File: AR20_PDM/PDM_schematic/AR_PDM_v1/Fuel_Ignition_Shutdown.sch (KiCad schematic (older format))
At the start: 22 parts, among them K1 DIPxx-1Cxx-51x, K2 DIPxx-1Cxx-51x, U11 N-MOS, U12 P-MOS, U13 N-MOS, U14 N-MOS, U29 INA233, U30 INA233

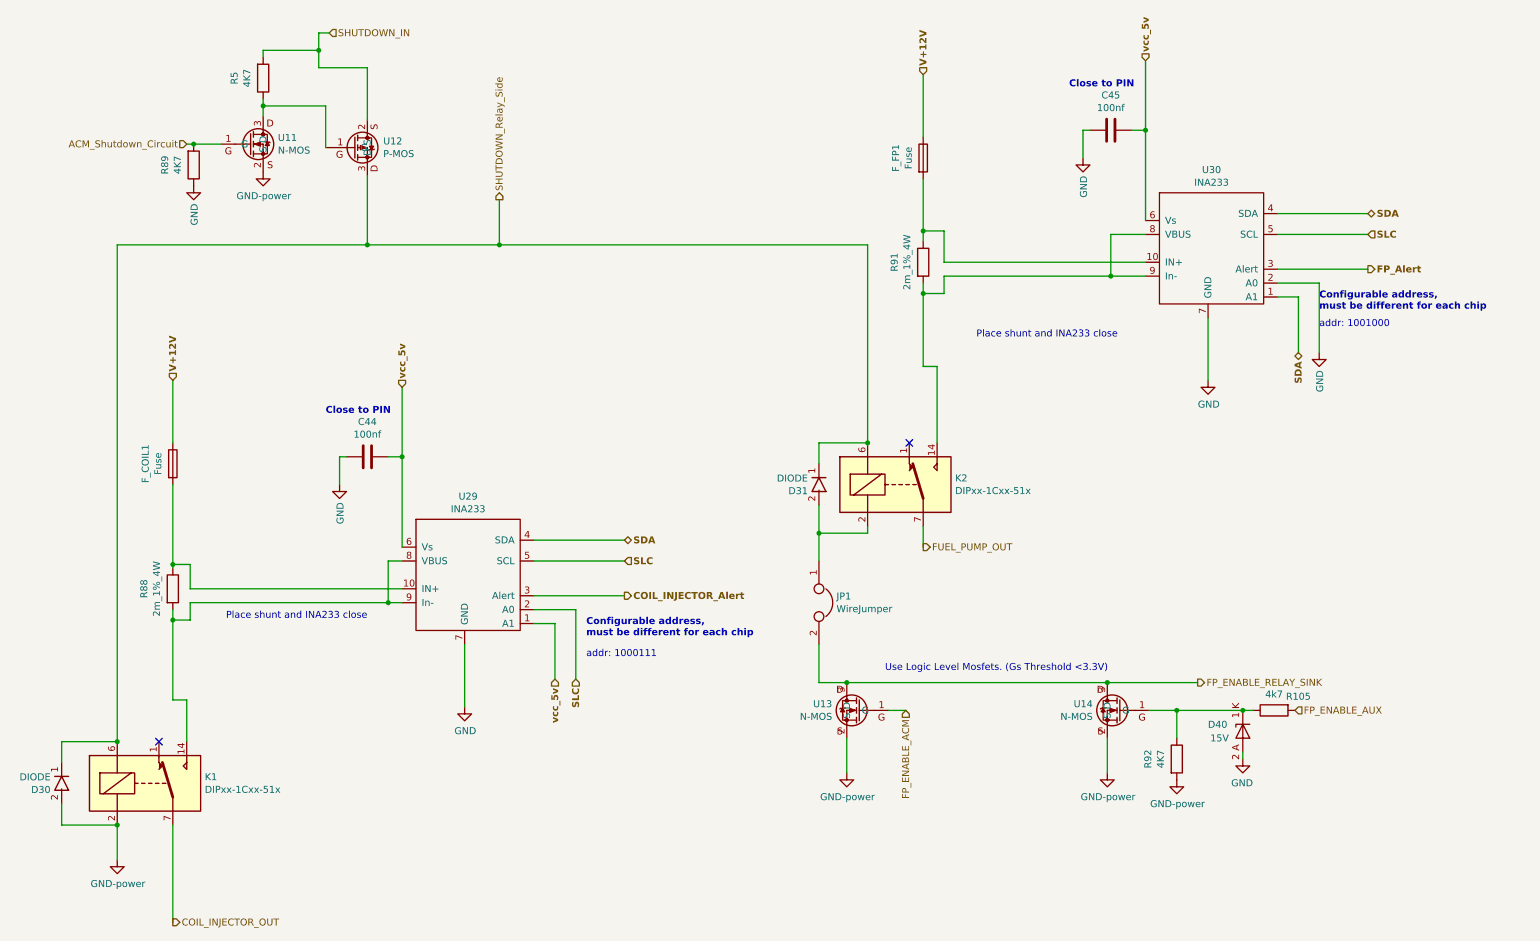
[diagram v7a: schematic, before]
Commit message: schematics rework
Fixed INA233 frying due to inductive flyback:
- Paced ina233 high side of the mosftets
- New input protection reseistors, and zener diodes, on each ina233.
Simplified:
- Removed the MUX and mos sense lines, as i realize that most of this functionality can be obtained trough INA233.
- Removed some of the cappacitors , besides the most needed ones.
- removed  back to back zener diode configuration, now a single diode insted.
 to reduce negative voltage in case of loss of VS, to be easy on the INA233 filters.
new stuff:
- Another temp sensor.
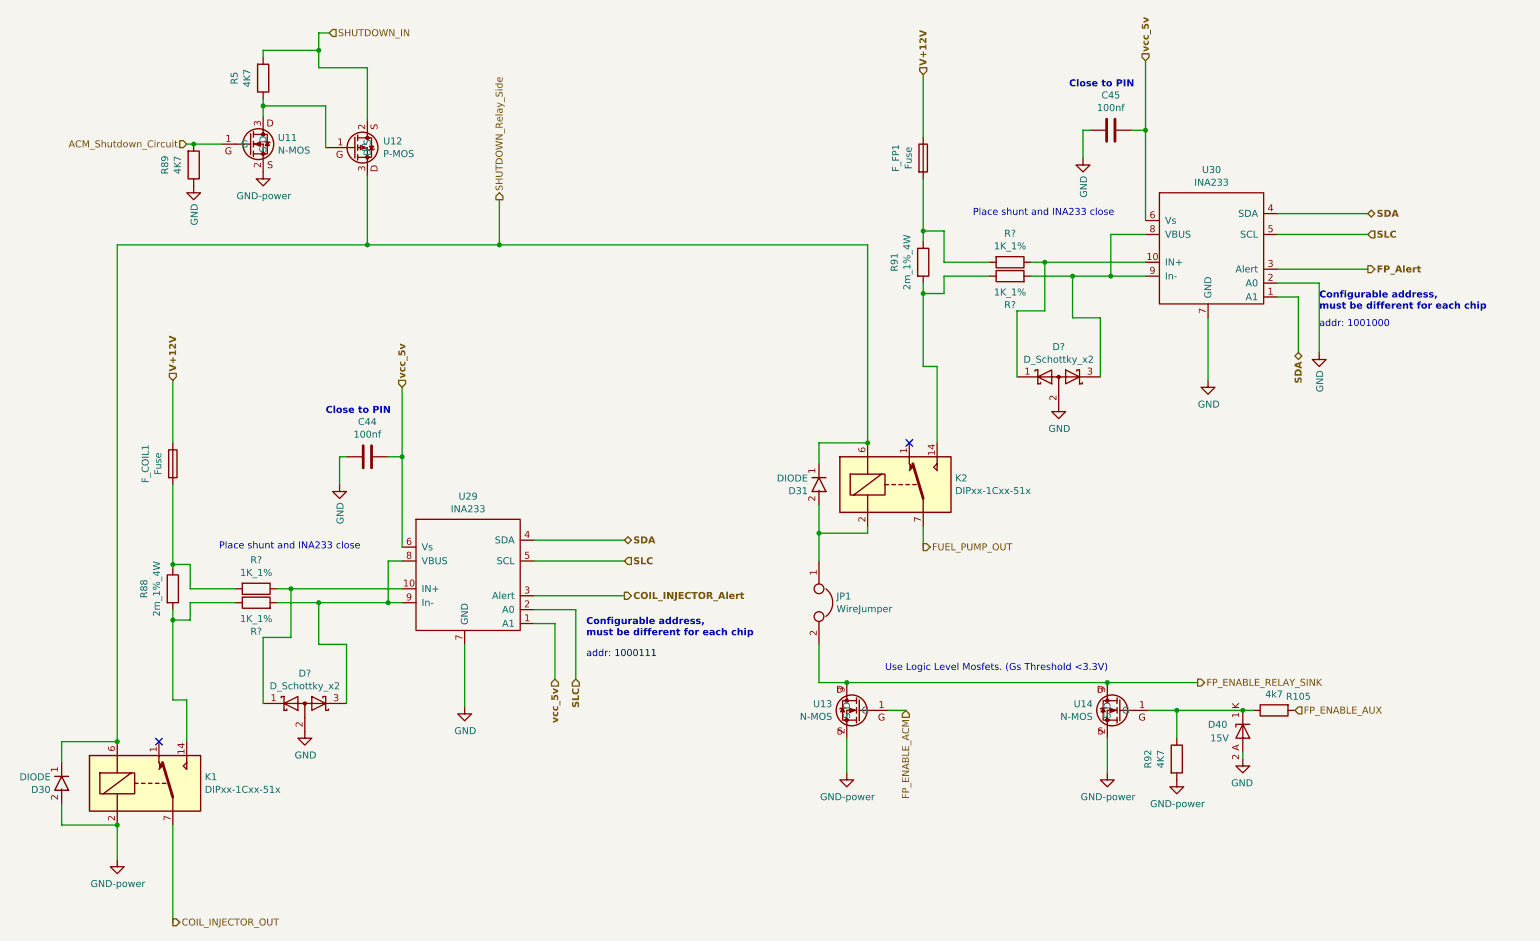
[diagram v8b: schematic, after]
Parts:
- added D? (x2): D_Schottky_x2, symbol AR20_PDM_v1-rescue:D_Schottky_x2
- added R? (x4): 1K_1%, Resistor_SMD:R_0603_1608Metric, symbol AR20_PDM_v1-rescue:R-Device
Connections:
- net GND: now also D?.2 (A), D?.2 (A)
- net at F_FP1.2, R91.1: now also R?.2; no longer U30.10 (IN+)
- net at F_COIL1.2, R88.1: now also R?.2; no longer U29.10 (IN+)
- net at U29.8 (VBUS), U29.9 (In-): now also D?.3 (K), R?.2; no longer K1.14, R88.2
- net at U30.8 (VBUS), U30.9 (In-): now also D?.3 (K), R?.2; no longer K2.14, R91.2
- new net: D?.1 (K), R?.1, U29.10 (IN+)
- new net: D?.1 (K), R?.1, U30.10 (IN+)
- new net: K2.14, R91.2, R?.1
- new net: K1.14, R88.2, R?.1
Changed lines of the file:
@@
 $Descr A4 11693 8268
 encoding utf-8
-Sheet 10 14
+Sheet 9 13
 Title ""
 Date ""
@@
 Wire Wire Line
 	1950 3650 1950 3200
-Text Notes 8750 2900 2    50   ~ 0
+Text Notes 8725 2025 2    50   ~ 0
 Place shunt and INA233 close \n
 Text HLabel 10025 5575 2    50   Input ~ 0
@@
 Text Notes 7075 5300 0    50   ~ 0
 Use Logic Level Mosfets. (Gs Threshold <3.3V)
-Text Notes 3350 4925 2    50   ~ 0
+Text Notes 3300 4425 2    50   ~ 0
 Place shunt and INA233 close \n
 Text HLabel 1950 3200 1    50   Input ~ 10
@@
 	1950 4925 1950 5500
 Wire Wire Line
-	3600 4700 2075 4700
-Wire Wire Line
 	2075 4700 2075 4525
 Wire Wire Line
@@
 Wire Wire Line
 	3500 4500 3500 4800
-Connection ~ 3500 4800
-Wire Wire Line
-	3500 4800 2075 4800
-Wire Wire Line
-	8950 2350 7500 2350
 Wire Wire Line
 	7500 2350 7500 2125
@@
 Wire Wire Line
 	8700 2150 8700 2450
-Connection ~ 8700 2450
-Wire Wire Line
-	8700 2450 7500 2450
 Text HLabel 7225 5575 3    50   Input ~ 0
 FP_ENABLE_ACM
@@
 Wire Wire Line
 	3350 950  3350 1325
+$Comp
+L AR20_PDM_v1-rescue:D_Schottky_x2 D?
+U 1 1 5EEF3E48
+P 8325 3175
+AR Path="/5DA89415/5EEF3E48" Ref="D?"  Part="1"
+AR Path="/5E10174B/5EEF3E48" Ref="D?"  Part="1"
+F 0 "D?" H 8325 3391 50  0000 C CNN
+F 1 "D_Schottky_x2" H 8325 3300 50  0000 C CNN
+F 2 "" H 8325 3175 50  0001 C CNN
+F 3 "~" H 8325 3175 50  0001 C CNN
+	1    8325 3175
+	1    0    0    -1
+$EndComp
+$Comp
+L AR20_PDM_v1-rescue:GND-power #PWR?
+U 1 1 5EEF3E4E
+P 8325 3375
+AR Path="/5DA89415/5EEF3E4E" Ref="#PWR?"  Part="1"
+AR Path="/5DEB10A1/5EEF3E4E" Ref="#PWR?"  Part="1"
+AR Path="/5DEB20EA/5EEF3E4E" Ref="#PWR?"  Part="1"
+AR Path="/5E0E4725/5EEF3E4E" Ref="#PWR?"  Part="1"
+AR Path="/5E0E4A93/5EEF3E4E" Ref="#PWR?"  Part="1"
+AR Path="/5E0E4EB5/5EEF3E4E" Ref="#PWR?"  Part="1"
+AR Path="/5E0E5304/5EEF3E4E" Ref="#PWR?"  Part="1"
+AR Path="/5E0E594B/5EEF3E4E" Ref="#PWR?"  Part="1"
+AR Path="/5E0E607C/5EEF3E4E" Ref="#PWR?"  Part="1"
+AR Path="/5E0FB5C8/5EEF3E4E" Ref="#PWR?"  Part="1"
+AR Path="/5E0FBBBD/5EEF3E4E" Ref="#PWR?"  Part="1"
+AR Path="/5E0FC3A2/5EEF3E4E" Ref="#PWR?"  Part="1"
+AR Path="/5E0FCFDC/5EEF3E4E" Ref="#PWR?"  Part="1"
+AR Path="/5E0FDCCC/5EEF3E4E" Ref="#PWR?"  Part="1"
+AR Path="/5E10174B/5EEF3E4E" Ref="#PWR?"  Part="1"
+F 0 "#PWR?" H 8325 3125 50  0001 C CNN
+F 1 "GND" H 8330 3202 50  0000 C CNN
+F 2 "" H 8325 3375 50  0001 C CNN
+F 3 "" H 8325 3375 50  0001 C CNN
+	1    8325 3375
+	1    0    0    -1
+$EndComp
+$Comp
+L AR20_PDM_v1-rescue:R-Device R?
+U 1 1 5EEF3E55
+P 7975 2350
+AR Path="/5DA89415/5EEF3E55" Ref="R?"  Part="1"
+AR Path="/5DEB10A1/5EEF3E55" Ref="R?"  Part="1"
+AR Path="/5DEB20EA/5EEF3E55" Ref="R?"  Part="1"
+AR Path="/5E0E4725/5EEF3E55" Ref="R?"  Part="1"
+AR Path="/5E0E4A93/5EEF3E55" Ref="R?"  Part="1"
+AR Path="/5E0E4EB5/5EEF3E55" Ref="R?"  Part="1"
+AR Path="/5E0E5304/5EEF3E55" Ref="R?"  Part="1"
+AR Path="/5E0E594B/5EEF3E55" Ref="R?"  Part="1"
+AR Path="/5E0E607C/5EEF3E55" Ref="R?"  Part="1"
+AR Path="/5E0FB5C8/5EEF3E55" Ref="R?"  Part="1"
+AR Path="/5E0FBBBD/5EEF3E55" Ref="R?"  Part="1"
+AR Path="/5E0FC3A2/5EEF3E55" Ref="R?"  Part="1"
+AR Path="/5E0FCFDC/5EEF3E55" Ref="R?"  Part="1"
+AR Path="/5E0FDCCC/5EEF3E55" Ref="R?"  Part="1"
+AR Path="/5E10174B/5EEF3E55" Ref="R?"  Part="1"
+F 0 "R?" V 7768 2350 50  0000 C CNN
+F 1 "1K_1%" V 7859 2350 50  0000 C CNN
+F 2 "Resistor_SMD:R_0603_1608Metric" V 7905 2350 50  0001 C CNN
+F 3 "~" H 7975 2350 50  0001 C CNN
+	1    7975 2350
+	0    1    1    0
+$EndComp
+$Comp
+L AR20_PDM_v1-rescue:R-Device R?
+U 1 1 5EEF3E5E
+P 7975 2450
+AR Path="/5DA89415/5EEF3E5E" Ref="R?"  Part="1"
+AR Path="/5DEB10A1/5EEF3E5E" Ref="R?"  Part="1"
+AR Path="/5DEB20EA/5EEF3E5E" Ref="R?"  Part="1"
+AR Path="/5E0E4725/5EEF3E5E" Ref="R?"  Part="1"
+AR Path="/5E0E4A93/5EEF3E5E" Ref="R?"  Part="1"
+AR Path="/5E0E4EB5/5EEF3E5E" Ref="R?"  Part="1"
+AR Path="/5E0E5304/5EEF3E5E" Ref="R?"  Part="1"
+AR Path="/5E0E594B/5EEF3E5E" Ref="R?"  Part="1"
+AR Path="/5E0E607C/5EEF3E5E" Ref="R?"  Part="1"
+AR Path="/5E0FB5C8/5EEF3E5E" Ref="R?"  Part="1"
+AR Path="/5E0FBBBD/5EEF3E5E" Ref="R?"  Part="1"
+AR Path="/5E0FC3A2/5EEF3E5E" Ref="R?"  Part="1"
+AR Path="/5E0FCFDC/5EEF3E5E" Ref="R?"  Part="1"
+AR Path="/5E0FDCCC/5EEF3E5E" Ref="R?"  Part="1"
+AR Path="/5E10174B/5EEF3E5E" Ref="R?"  Part="1"
+F 0 "R?" V 7768 2450 50  0000 C CNN
+F 1 "1K_1%" V 7859 2450 50  0000 C CNN
+F 2 "Resistor_SMD:R_0603_1608Metric" V 7905 2450 50  0001 C CNN
+F 3 "~" H 7975 2450 50  0001 C CNN
+	1    7975 2450
+	0    -1   -1   0
+$EndComp
+Connection ~ 8700 2450
+Wire Wire Line
+	8700 2450 8425 2450
+Wire Wire Line
+	8950 2350 8225 2350
+Wire Wire Line
+	7825 2350 7500 2350
+Wire Wire Line
+	7825 2450 7500 2450
+Wire Wire Line
+	8025 3175 8025 2700
+Wire Wire Line
+	8025 2700 8225 2700
+Wire Wire Line
+	8225 2700 8225 2350
+Connection ~ 8225 2350
+Wire Wire Line
+	8225 2350 8125 2350
+Wire Wire Line
+	8625 3175 8625 2750
+Wire Wire Line
+	8625 2750 8425 2750
+Wire Wire Line
+	8425 2750 8425 2450
+Connection ~ 8425 2450
+Wire Wire Line
+	8425 2450 8125 2450
+$Comp
+L AR20_PDM_v1-rescue:D_Schottky_x2 D?
+U 1 1 5EF32925
+P 2900 5525
+AR Path="/5DA89415/5EF32925" Ref="D?"  Part="1"
+AR Path="/5E10174B/5EF32925" Ref="D?"  Part="1"
+F 0 "D?" H 2900 5741 50  0000 C CNN
+F 1 "D_Schottky_x2" H 2900 5650 50  0000 C CNN
+F 2 "" H 2900 5525 50  0001 C CNN
+F 3 "~" H 2900 5525 50  0001 C CNN
+	1    2900 5525
+	1    0    0    -1
+$EndComp
+$Comp
+L AR20_PDM_v1-rescue:GND-power #PWR?
+U 1 1 5EF3292B
+P 2900 5725
+AR Path="/5DA89415/5EF3292B" Ref="#PWR?"  Part="1"
+AR Path="/5DEB10A1/5EF3292B" Ref="#PWR?"  Part="1"
+AR Path="/5DEB20EA/5EF3292B" Ref="#PWR?"  Part="1"
+AR Path="/5E0E4725/5EF3292B" Ref="#PWR?"  Part="1"
+AR Path="/5E0E4A93/5EF3292B" Ref="#PWR?"  Part="1"
+AR Path="/5E0E4EB5/5EF3292B" Ref="#PWR?"  Part="1"
+AR Path="/5E0E5304/5EF3292B" Ref="#PWR?"  Part="1"
+AR Path="/5E0E594B/5EF3292B" Ref="#PWR?"  Part="1"
+AR Path="/5E0E607C/5EF3292B" Ref="#PWR?"  Part="1"
+AR Path="/5E0FB5C8/5EF3292B" Ref="#PWR?"  Part="1"
+AR Path="/5E0FBBBD/5EF3292B" Ref="#PWR?"  Part="1"
+AR Path="/5E0FC3A2/5EF3292B" Ref="#PWR?"  Part="1"
+AR Path="/5E0FCFDC/5EF3292B" Ref="#PWR?"  Part="1"
+AR Path="/5E0FDCCC/5EF3292B" Ref="#PWR?"  Part="1"
+AR Path="/5E10174B/5EF3292B" Ref="#PWR?"  Part="1"
+F 0 "#PWR?" H 2900 5475 50  0001 C CNN
+F 1 "GND" H 2905 5552 50  0000 C CNN
+F 2 "" H 2900 5725 50  0001 C CNN
+F 3 "" H 2900 5725 50  0001 C CNN
+	1    2900 5725
+	1    0    0    -1
+$EndComp
+$Comp
+L AR20_PDM_v1-rescue:R-Device R?
+U 1 1 5EF32931
+P 2550 4700
+AR Path="/5DA89415/5EF32931" Ref="R?"  Part="1"
+AR Path="/5DEB10A1/5EF32931" Ref="R?"  Part="1"
+AR Path="/5DEB20EA/5EF32931" Ref="R?"  Part="1"
+AR Path="/5E0E4725/5EF32931" Ref="R?"  Part="1"
+AR Path="/5E0E4A93/5EF32931" Ref="R?"  Part="1"
+AR Path="/5E0E4EB5/5EF32931" Ref="R?"  Part="1"
+AR Path="/5E0E5304/5EF32931" Ref="R?"  Part="1"
+AR Path="/5E0E594B/5EF32931" Ref="R?"  Part="1"
+AR Path="/5E0E607C/5EF32931" Ref="R?"  Part="1"
+AR Path="/5E0FB5C8/5EF32931" Ref="R?"  Part="1"
+AR Path="/5E0FBBBD/5EF32931" Ref="R?"  Part="1"
+AR Path="/5E0FC3A2/5EF32931" Ref="R?"  Part="1"
+AR Path="/5E0FCFDC/5EF32931" Ref="R?"  Part="1"
+AR Path="/5E0FDCCC/5EF32931" Ref="R?"  Part="1"
+AR Path="/5E10174B/5EF32931" Ref="R?"  Part="1"
+F 0 "R?" V 2343 4700 50  0000 C CNN
+F 1 "1K_1%" V 2434 4700 50  0000 C CNN
+F 2 "Resistor_SMD:R_0603_1608Metric" V 2480 4700 50  0001 C CNN
+F 3 "~" H 2550 4700 50  0001 C CNN
+	1    2550 4700
+	0    1    1    0
+$EndComp
+$Comp
+L AR20_PDM_v1-rescue:R-Device R?
+U 1 1 5EF32937
+P 2550 4800
+AR Path="/5DA89415/5EF32937" Ref="R?"  Part="1"
+AR Path="/5DEB10A1/5EF32937" Ref="R?"  Part="1"
+AR Path="/5DEB20EA/5EF32937" Ref="R?"  Part="1"
+AR Path="/5E0E4725/5EF32937" Ref="R?"  Part="1"
+AR Path="/5E0E4A93/5EF32937" Ref="R?"  Part="1"
+AR Path="/5E0E4EB5/5EF32937" Ref="R?"  Part="1"
+AR Path="/5E0E5304/5EF32937" Ref="R?"  Part="1"
+AR Path="/5E0E594B/5EF32937" Ref="R?"  Part="1"
+AR Path="/5E0E607C/5EF32937" Ref="R?"  Part="1"
+AR Path="/5E0FB5C8/5EF32937" Ref="R?"  Part="1"
+AR Path="/5E0FBBBD/5EF32937" Ref="R?"  Part="1"
+AR Path="/5E0FC3A2/5EF32937" Ref="R?"  Part="1"
+AR Path="/5E0FCFDC/5EF32937" Ref="R?"  Part="1"
+AR Path="/5E0FDCCC/5EF32937" Ref="R?"  Part="1"
+AR Path="/5E10174B/5EF32937" Ref="R?"  Part="1"
+F 0 "R?" V 2343 4800 50  0000 C CNN
+F 1 "1K_1%" V 2434 4800 50  0000 C CNN
+F 2 "Resistor_SMD:R_0603_1608Metric" V 2480 4800 50  0001 C CNN
+F 3 "~" H 2550 4800 50  0001 C CNN
+	1    2550 4800
+	0    -1   -1   0
+$EndComp
+Wire Wire Line
+	2400 4700 2075 4700
+Wire Wire Line
+	2400 4800 2075 4800
+Wire Wire Line
+	2600 5525 2600 5050
+Wire Wire Line
+	2600 5050 2800 5050
+Wire Wire Line
+	2800 5050 2800 4700
+Connection ~ 2800 4700
+Wire Wire Line
+	2800 4700 2700 4700
+Wire Wire Line
+	3200 5100 3000 5100
+Wire Wire Line
+	3000 5100 3000 4800
+Connection ~ 3000 4800
+Wire Wire Line
+	3000 4800 2700 4800
+Wire Wire Line
+	3200 5100 3200 5525
+Wire Wire Line
+	2800 4700 3600 4700
+Wire Wire Line
+	3000 4800 3500 4800
+Connection ~ 3500 4800
 $EndSCHEMATC
